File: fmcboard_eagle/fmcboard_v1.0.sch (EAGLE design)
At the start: 51 parts, among them IC1 OPA699ID, IC2 OPA699ID, IC3 ICL7660CPA, IC4 ICL7660CPA, IC5 LM358, J1 8pin, J12 4p-2.54, J2 ASP-134604-01, J3 4p-2.54, J4 4p-2.54, J5 8pin, U1 TXS0108EPWR

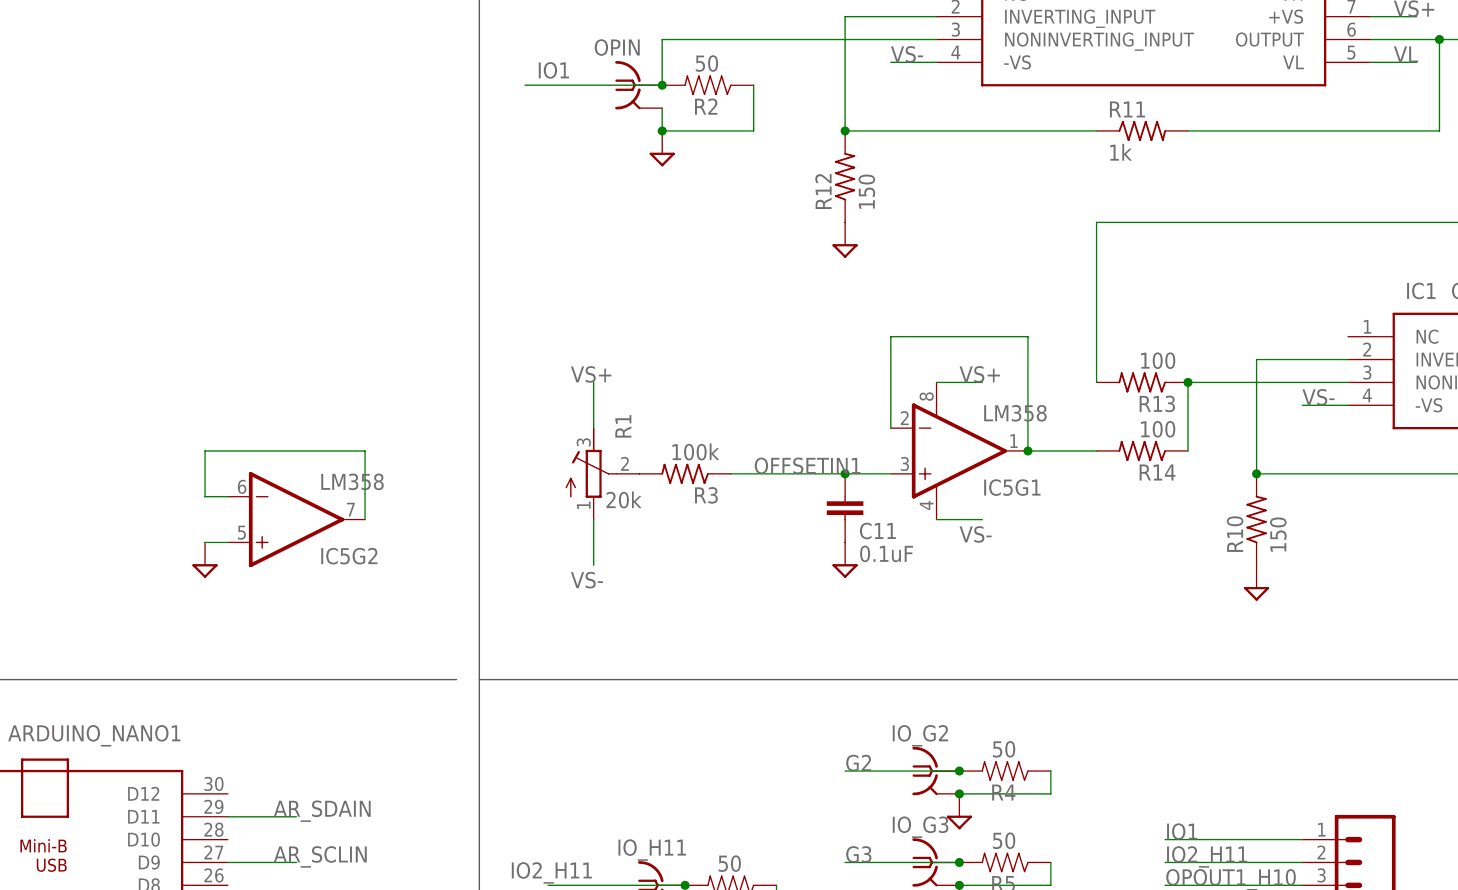
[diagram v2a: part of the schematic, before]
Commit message: Update gain resistor values
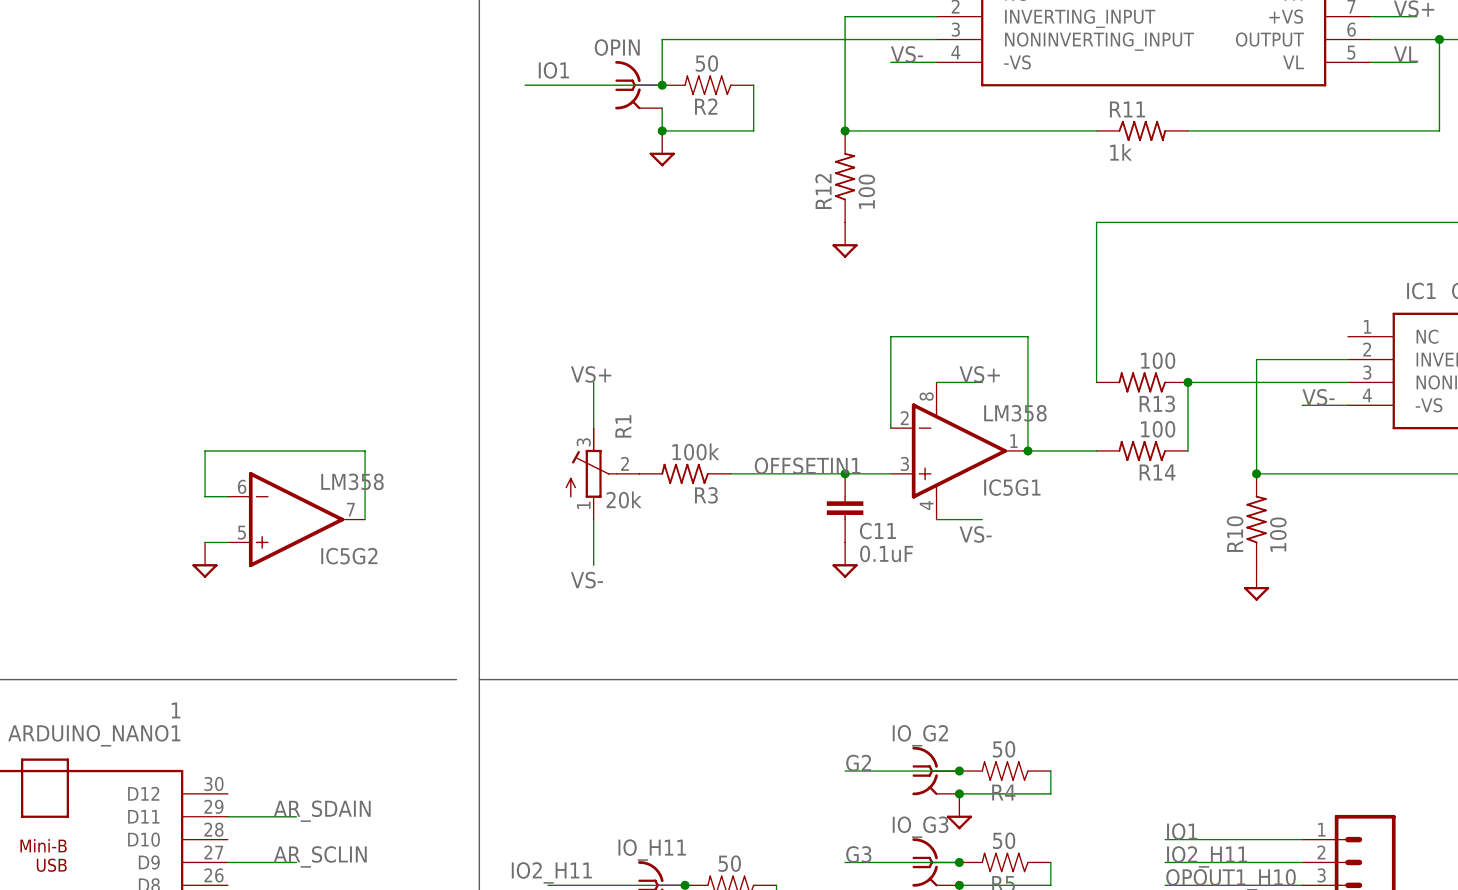
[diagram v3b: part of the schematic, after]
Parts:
- ARDUINO_NANO1: value (none) -> 1
- R10, R12: value 150 -> 100
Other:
- note added: "x10 /2 gain"
- note added: "x10 gain"
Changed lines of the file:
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@@
 <part name="SUPPLY23" library="supply2" library_urn="urn:adsk.eagle:library:372" deviceset="GND" device=""/>
 <part name="SUPPLY24" library="supply2" library_urn="urn:adsk.eagle:library:372" deviceset="GND" device=""/>
-<part name="ARDUINO_NANO1" library="ArduinoNanoV30" deviceset="ARDUINO_NANO" device=""/>
+<part name="ARDUINO_NANO1" library="ArduinoNanoV30" deviceset="ARDUINO_NANO" device="" value="1"/>
 <part name="R9" library="rcl" library_urn="urn:adsk.eagle:library:334" deviceset="R-US_" device="R0805" package3d_urn="urn:adsk.eagle:package:23553/2" value="1k"/>
-<part name="R10" library="rcl" library_urn="urn:adsk.eagle:library:334" deviceset="R-US_" device="R0805" package3d_urn="urn:adsk.eagle:package:23553/2" value="150"/>
+<part name="R10" library="rcl" library_urn="urn:adsk.eagle:library:334" deviceset="R-US_" device="R0805" package3d_urn="urn:adsk.eagle:package:23553/2" value="100"/>
 <part name="R11" library="rcl" library_urn="urn:adsk.eagle:library:334" deviceset="R-US_" device="R0805" package3d_urn="urn:adsk.eagle:package:23553/2" value="1k"/>
-<part name="R12" library="rcl" library_urn="urn:adsk.eagle:library:334" deviceset="R-US_" device="R0805" package3d_urn="urn:adsk.eagle:package:23553/2" value="150"/>
+<part name="R12" library="rcl" library_urn="urn:adsk.eagle:library:334" deviceset="R-US_" device="R0805" package3d_urn="urn:adsk.eagle:package:23553/2" value="100"/>
 <part name="R13" library="rcl" library_urn="urn:adsk.eagle:library:334" deviceset="R-US_" device="R0805" package3d_urn="urn:adsk.eagle:package:23553/2" value="100"/>
 <part name="R14" library="rcl" library_urn="urn:adsk.eagle:library:334" deviceset="R-US_" device="R0805" package3d_urn="urn:adsk.eagle:package:23553/2" value="100"/>
@@
 <text x="-83.82" y="104.14" size="1.778" layer="90">Arduino</text>
 <text x="-22.86" y="114.3" size="1.778" layer="90">Extra op amp</text>
+<text x="53.34" y="162.56" size="1.778" layer="90">x10 gain</text>
+<text x="101.6" y="124.46" size="1.778" layer="90">x10 /2 gain</text>
 </plain>
 <instances>

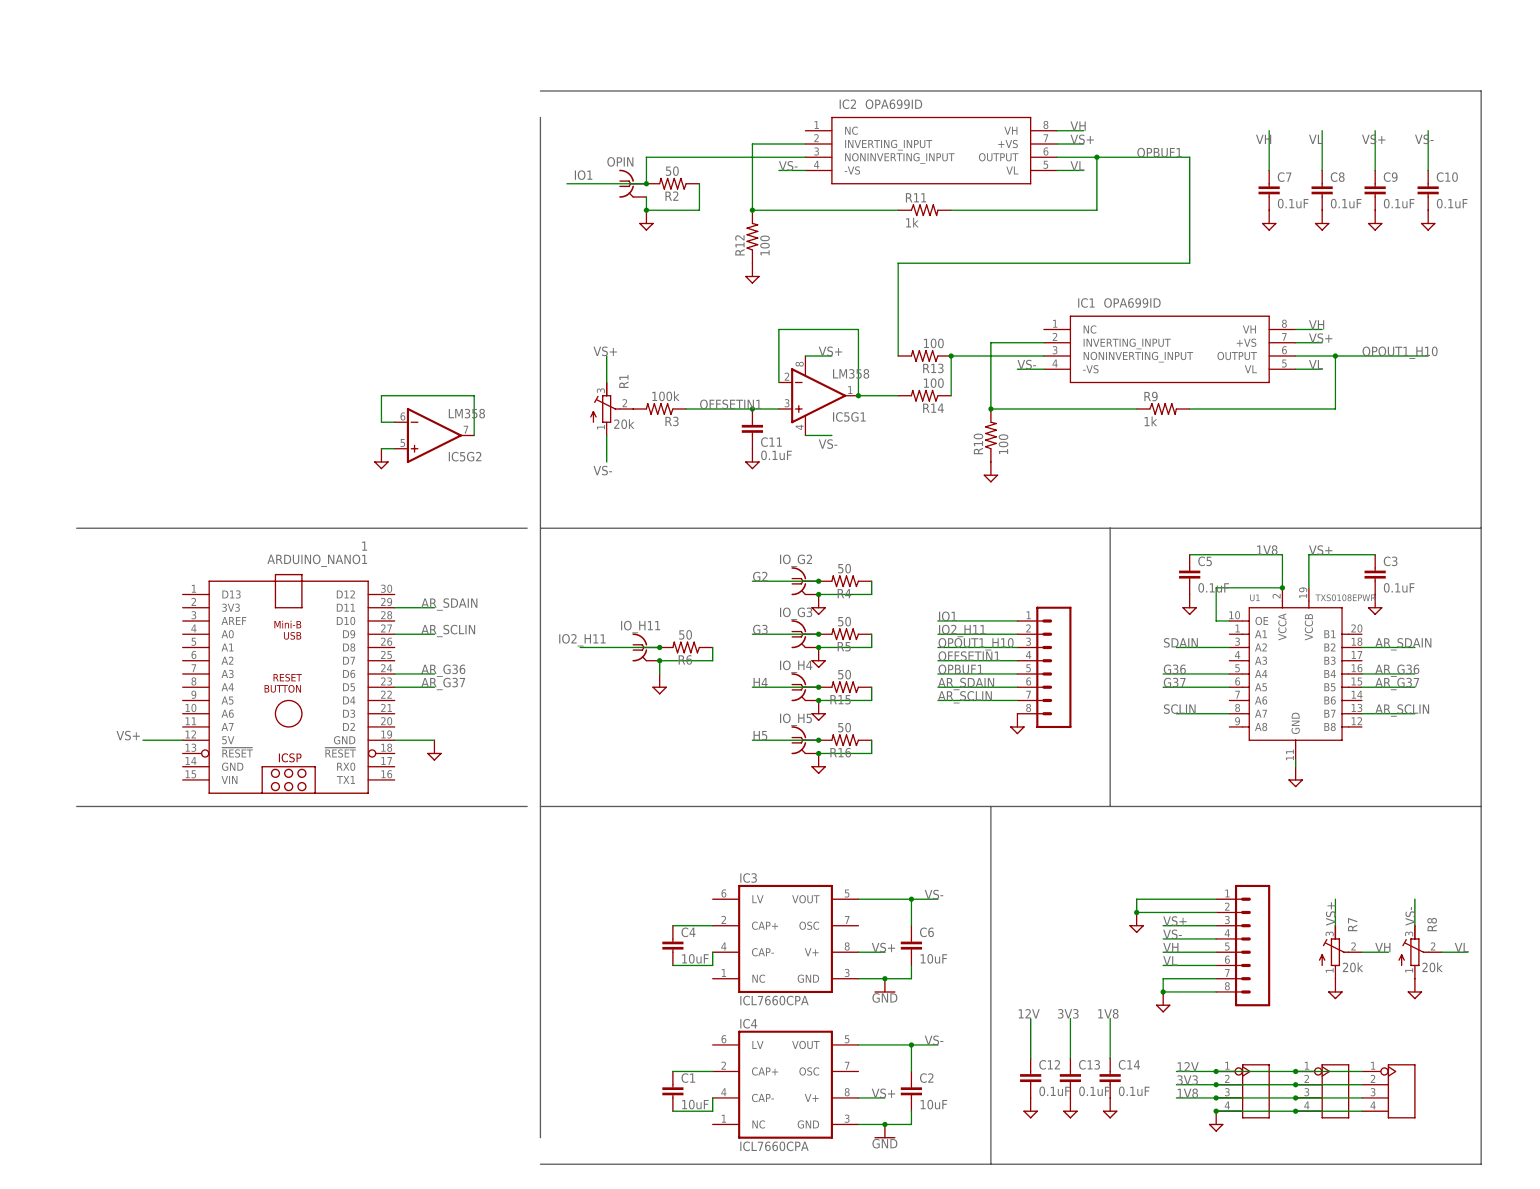
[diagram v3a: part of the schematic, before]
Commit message: use bss138 level shifting
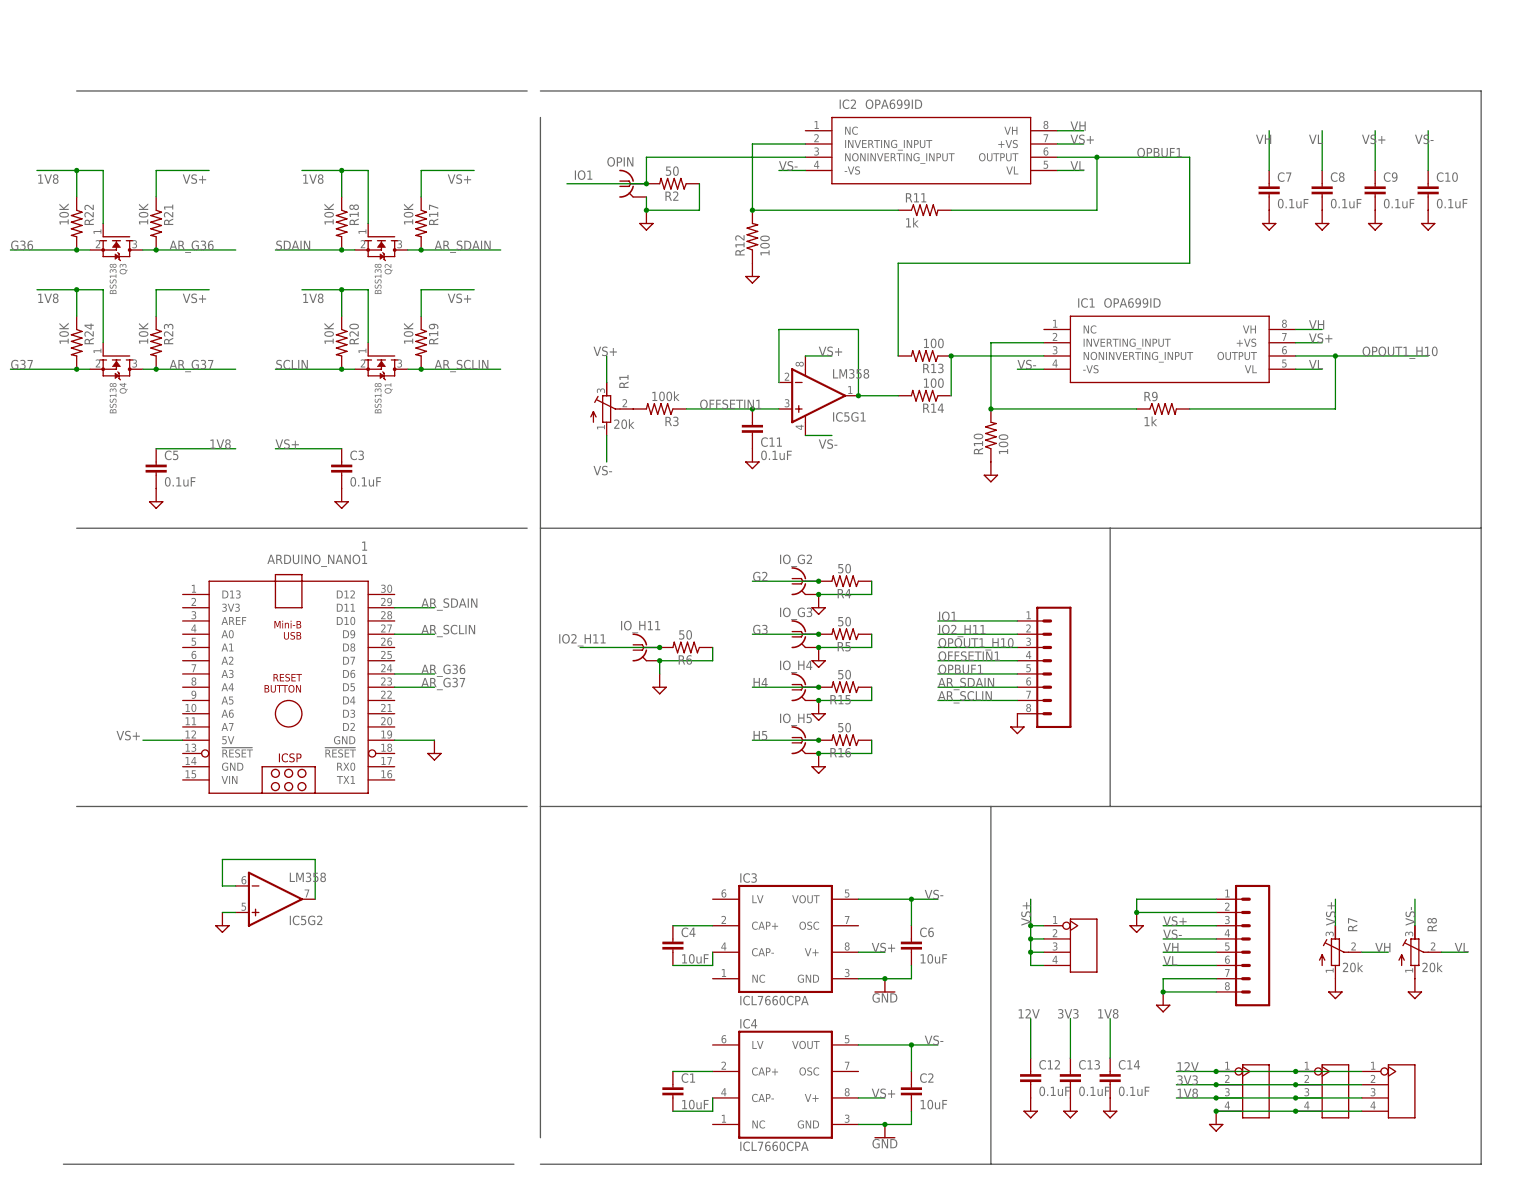
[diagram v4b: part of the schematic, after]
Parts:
- removed U1: TXS0108EPWR, Seeed-IC:LOGIC-TXS0108EPWR(TSSOP20)
- added J6: 4p-2.54, Seeed-Connector:DIP-BLACK-FEMALE-HEADER-VERT(4P-2.54)
- added Q1, Q2, Q3, Q4: BSS138, adafruit:MOSFET-NREFLOW
- added R17, R18, R19, R20, R21, R22, R23, R24: 10K, adafruit:R-US_R0805
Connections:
- net 1V8: now also Q1.G, Q2.G, Q3.G, Q4.G, R18.1, R20.1, R22.1, R24.1; no longer U1.OE, U1.VCCA
- net AR_G36: now also Q3.D, R21.2; no longer U1.B4
- net AR_G37: now also Q4.D, R23.2; no longer U1.B5
- net AR_SCLIN: now also Q1.D, R19.2; no longer U1.B7
- net AR_SDAIN: now also Q2.D, R17.2; no longer U1.B2
- net G36: now also Q3.S, R22.2; no longer U1.A4
- net G37: now also Q4.S, R24.2; no longer U1.A5
- net GND: no longer U1.GND
- net SCLIN: now also Q1.S, R20.2; no longer U1.A7
- net SDAIN: now also Q2.S, R18.2; no longer U1.A2
- net VS+: now also J6.P$1, J6.P$2, J6.P$3, J6.P$4, R17.1, R19.1, R21.1, R23.1; no longer U1.VCCB
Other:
- note added: "Level shifters (bss138 based)"
- note removed: "Level shifter"
- moved on the sheet: C3, C5, IC5G2
